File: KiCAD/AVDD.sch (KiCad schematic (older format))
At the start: 5 parts, among them J29 Conn_01x03, J30 Conn_01x03, U10 LP5907

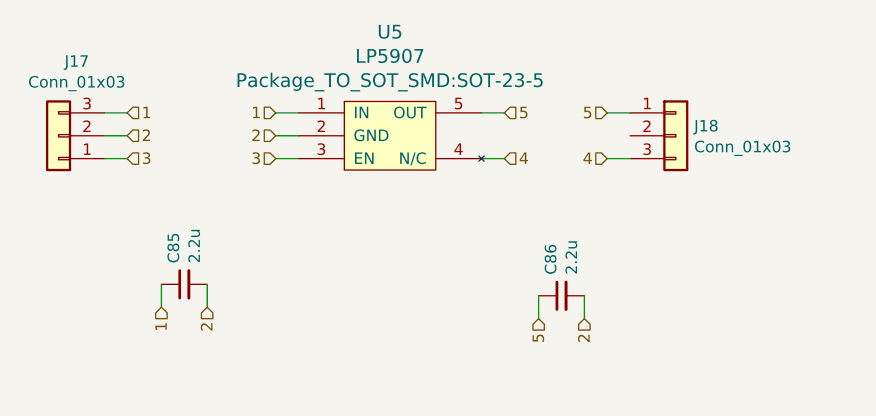
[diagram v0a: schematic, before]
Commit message: added usb, crystals
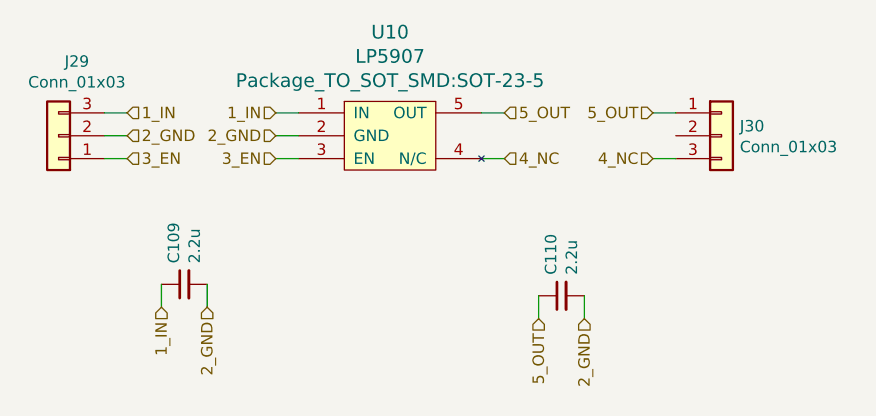
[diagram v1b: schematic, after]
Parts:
- renumbered C109 to C85, C110 to C86, J29 to J17, J30 to J18, U10 to U5
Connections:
- net 1 renamed 1_IN
- net 2 renamed 2_GND
- net 3 renamed 3_EN
- net 4 renamed 4_NC
- net 5 renamed 5_OUT
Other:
- moved on the sheet: J30
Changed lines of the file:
@@
 $Descr A4 11693 8268
 encoding utf-8
-Sheet 7 17
+Sheet 7 18
 Title ""
 Date ""
@@
 $EndDescr
 Text HLabel 2300 2750 3    50   Input ~ 0
-1
+1_IN
 Text HLabel 2500 2750 3    50   Input ~ 0
-2
+2_GND
 Text HLabel 3950 2800 3    50   Input ~ 0
-5
+5_OUT
 Text HLabel 4150 2800 3    50   Input ~ 0
-2
+2_GND
 Wire Wire Line
 	3950 2800 3950 2700
@@
 AR Path="/5CE92455/5CDAC673" Ref="C?"  Part="1"
 AR Path="/5CDAC673" Ref="C?"  Part="1"
-AR Path="/5CDAC31F/5CDAC673" Ref="C110"  Part="1"
+AR Path="/5CDAC31F/5CDAC673" Ref="C86"  Part="1"
 AR Path="/5CDACBFB/5CDAC673" Ref="C88"  Part="1"
-AR Path="/5D23D721/5CDAC673" Ref="C86"  Part="1"
-F 0 "C86" H 4142 2746 50  0000 L CNN
+AR Path="/5D23D721/5CDAC673" Ref="C110"  Part="1"
+F 0 "C110" H 4142 2746 50  0000 L CNN
 F 1 "2.2u" H 4142 2655 50  0000 L CNN
 F 2 "Capacitor_SMD:C_0603_1608Metric" H 4050 2700 50  0001 C CNN
@@
 $EndComp
 Wire Wire Line
-	4250 1900 4350 1900
-Text HLabel 4250 1900 0    50   Input ~ 0
-5
+	4450 1900 4550 1900
+Text HLabel 4450 1900 0    50   Input ~ 0
+5_OUT
 Wire Wire Line
 	2150 2100 2050 2100
 Text HLabel 2150 2100 2    50   Input ~ 0
-3
+3_EN
 Wire Wire Line
 	2150 2000 2050 2000
 Text HLabel 2150 2000 2    50   Input ~ 0
-2
+2_GND
 Wire Wire Line
 	2150 1900 2050 1900
 Text HLabel 2150 1900 2    50   Input ~ 0
-1
+1_IN
 Wire Wire Line
 	3800 1900 3700 1900
 Text HLabel 3800 1900 2    50   Input ~ 0
-5
+5_OUT
 Wire Wire Line
 	2500 2750 2500 2650
@@
 AR Path="/5CE92455/5CDAC686" Ref="C?"  Part="1"
 AR Path="/5CDAC686" Ref="C?"  Part="1"
-AR Path="/5CDAC31F/5CDAC686" Ref="C109"  Part="1"
+AR Path="/5CDAC31F/5CDAC686" Ref="C85"  Part="1"
 AR Path="/5CDACBFB/5CDAC686" Ref="C87"  Part="1"
-AR Path="/5D23D721/5CDAC686" Ref="C85"  Part="1"
-F 0 "C85" H 2492 2696 50  0000 L CNN
+AR Path="/5D23D721/5CDAC686" Ref="C109"  Part="1"
+F 0 "C109" H 2492 2696 50  0000 L CNN
 F 1 "2.2u" H 2492 2605 50  0000 L CNN
 F 2 "Capacitor_SMD:C_0603_1608Metric" H 2400 2650 50  0001 C CNN
@@
 	2800 2100 2900 2100
 Text HLabel 2800 2100 0    50   Input ~ 0
-3
+3_EN
 Wire Wire Line
 	2800 2000 2900 2000
 Text HLabel 2800 2000 0    50   Input ~ 0
-2
+2_GND
 Wire Wire Line
 	2800 1900 2900 1900
 Text HLabel 2800 1900 0    50   Input ~ 0
-1
+1_IN
 $Comp
 L Connector_Generic:Conn_01x03 J?
@@
 P 1850 2000
 AR Path="/5CDAC693" Ref="J?"  Part="1"
-AR Path="/5CDAC31F/5CDAC693" Ref="J29"  Part="1"
+AR Path="/5CDAC31F/5CDAC693" Ref="J17"  Part="1"
 AR Path="/5CDACBFB/5CDAC693" Ref="J19"  Part="1"
-AR Path="/5D23D721/5CDAC693" Ref="J17"  Part="1"
-F 0 "J17" H 1770 1675 50  0000 C CNN
+AR Path="/5D23D721/5CDAC693" Ref="J29"  Part="1"
+F 0 "J29" H 1770 1675 50  0000 C CNN
 F 1 "Conn_01x03" H 1770 1766 50  0000 C CNN
 F 2 "Connector_PinHeader_2.54mm:PinHeader_1x03_P2.54mm_Vertical" H 1850 2000 50  0001 C CNN
@@
 L Connector_Generic:Conn_01x03 J?
 U 1 1 5CDAC69A
-P 4550 2000
+P 4750 2000
 AR Path="/5CDAC69A" Ref="J?"  Part="1"
-AR Path="/5CDAC31F/5CDAC69A" Ref="J30"  Part="1"
+AR Path="/5CDAC31F/5CDAC69A" Ref="J18"  Part="1"
 AR Path="/5CDACBFB/5CDAC69A" Ref="J20"  Part="1"
-AR Path="/5D23D721/5CDAC69A" Ref="J18"  Part="1"
-F 0 "J18" H 4630 2042 50  0000 L CNN
-F 1 "Conn_01x03" H 4630 1951 50  0000 L CNN
-F 2 "Connector_PinHeader_2.54mm:PinHeader_1x03_P2.54mm_Vertical" H 4550 2000 50  0001 C CNN
-F 3 "~" H 4550 2000 50  0001 C CNN
-	1    4550 2000
+AR Path="/5D23D721/5CDAC69A" Ref="J30"  Part="1"
+F 0 "J30" H 4830 2042 50  0000 L CNN
+F 1 "Conn_01x03" H 4830 1951 50  0000 L CNN
+F 2 "Connector_PinHeader_2.54mm:PinHeader_1x03_P2.54mm_Vertical" H 4750 2000 50  0001 C CNN
+F 3 "~" H 4750 2000 50  0001 C CNN
+	1    4750 2000
 	1    0    0    -1
 $EndComp
@@
 P 3300 2000
 AR Path="/5CDAC6A1" Ref="U?"  Part="1"
-AR Path="/5CDAC31F/5CDAC6A1" Ref="U10"  Part="1"
+AR Path="/5CDAC31F/5CDAC6A1" Ref="U5"  Part="1"
 AR Path="/5CDACBFB/5CDAC6A1" Ref="U6"  Part="1"
-AR Path="/5D23D721/5CDAC6A1" Ref="U5"  Part="1"
-F 0 "U5" H 3300 2453 60  0000 C CNN
+AR Path="/5D23D721/5CDAC6A1" Ref="U10"  Part="1"
+F 0 "U10" H 3300 2453 60  0000 C CNN
 F 1 "LP5907" H 3300 2347 60  0000 C CNN
 F 2 "Package_TO_SOT_SMD:SOT-23-5" H 3300 2241 60  0000 C CNN
@@
 $EndComp
 Wire Wire Line
-	4250 2100 4350 2100
-Text HLabel 4250 2100 0    50   Input ~ 0
-4
+	4450 2100 4550 2100
+Text HLabel 4450 2100 0    50   Input ~ 0
+4_NC
 Wire Wire Line
 	3800 2100 3700 2100
 Text HLabel 3800 2100 2    50   Input ~ 0
-4
+4_NC
 $EndSCHEMATC
